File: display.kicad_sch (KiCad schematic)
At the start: 32 parts, among them Q1 AO3401A, Q2 BSS138

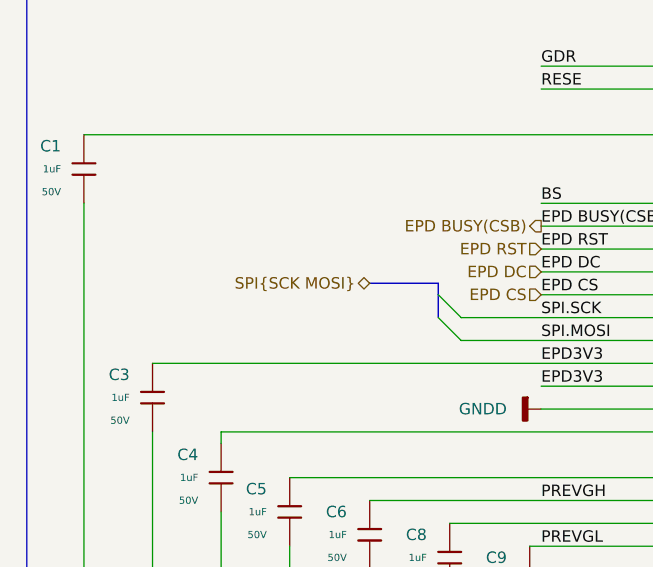
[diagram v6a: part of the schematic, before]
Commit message: Changed some parts for more common ones
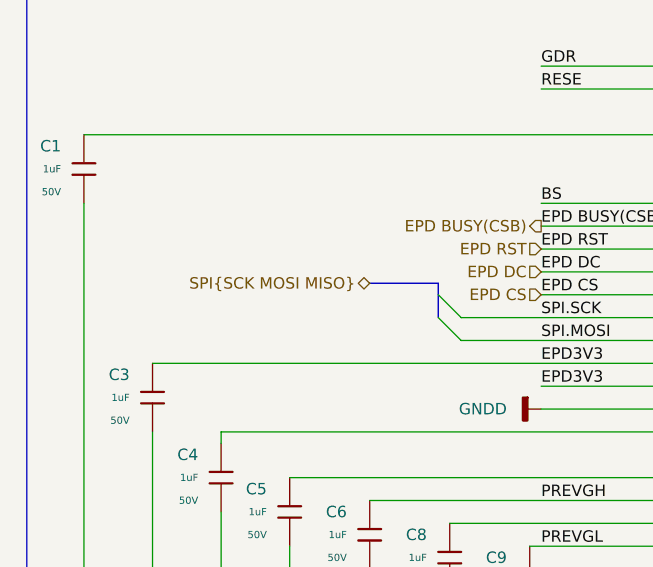
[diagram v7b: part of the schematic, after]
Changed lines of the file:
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@@
 		)
 	)
-	(hierarchical_label "SPI{SCK MOSI}"
+	(hierarchical_label "SPI{SCK MOSI MISO}"
 		(shape bidirectional)
 		(at 55.88 152.4 180)
@@
 		(dnp no)
 		(fields_autoplaced yes)
-		(property "Reference" "#PWR02"
+		(property "Reference" "#PWR03"
 			(at 49.53 118.11 0)
 			(effects
@@
 			(project "E-paper-picture-frame-HW"
 				(path "/84f37c25-92ec-4cd3-b0ad-d93e10e73cdb/9b514820-994d-4acc-ba3e-efc41ebe2f4e"
-					(reference "#PWR02")
+					(reference "#PWR03")
 					(unit 1)
 				)
@@
 		(dnp no)
 		(fields_autoplaced yes)
-		(property "Reference" "#PWR08"
+		(property "Reference" "#PWR09"
 			(at 95.25 33.02 0)
 			(effects
@@
 			(project ""
 				(path "/84f37c25-92ec-4cd3-b0ad-d93e10e73cdb/9b514820-994d-4acc-ba3e-efc41ebe2f4e"
-					(reference "#PWR08")
+					(reference "#PWR09")
 					(unit 1)
 				)
@@
 		(dnp no)
 		(fields_autoplaced yes)
-		(property "Reference" "#PWR06"
+		(property "Reference" "#PWR07"
 			(at 80.01 66.04 0)
 			(effects
@@
 			(project "E-paper-picture-frame-HW"
 				(path "/84f37c25-92ec-4cd3-b0ad-d93e10e73cdb/9b514820-994d-4acc-ba3e-efc41ebe2f4e"
-					(reference "#PWR06")
+					(reference "#PWR07")
 					(unit 1)
 				)
@@
 		(dnp no)
 		(fields_autoplaced yes)
-		(property "Reference" "#PWR011"
+		(property "Reference" "#PWR012"
 			(at 109.22 57.15 0)
 			(effects
@@
 			(project "E-paper-picture-frame-HW"
 				(path "/84f37c25-92ec-4cd3-b0ad-d93e10e73cdb/9b514820-994d-4acc-ba3e-efc41ebe2f4e"
-					(reference "#PWR011")
+					(reference "#PWR012")
 					(unit 1)
 				)
@@
 		(dnp no)
 		(fields_autoplaced yes)
-		(property "Reference" "#PWR04"
+		(property "Reference" "#PWR05"
 			(at 58.42 198.12 0)
 			(effects
@@
 			(project "E-paper-picture-frame-HW"
 				(path "/84f37c25-92ec-4cd3-b0ad-d93e10e73cdb/9b514820-994d-4acc-ba3e-efc41ebe2f4e"
-					(reference "#PWR04")
+					(reference "#PWR05")
 					(unit 1)
 				)
@@
 		(on_board yes)
 		(dnp no)
-		(property "Reference" "#PWR09"
+		(property "Reference" "#PWR010"
 			(at 105.41 114.3 0)
 			(effects
@@
 			(project "E-paper-picture-frame-HW"
 				(path "/84f37c25-92ec-4cd3-b0ad-d93e10e73cdb/9b514820-994d-4acc-ba3e-efc41ebe2f4e"
-					(reference "#PWR09")
+					(reference "#PWR010")
 					(unit 1)
 				)
@@
 		(dnp no)
 		(fields_autoplaced yes)
-		(property "Reference" "#PWR012"
+		(property "Reference" "#PWR013"
 			(at 143.51 46.99 0)
 			(effects
@@
 			(project "E-paper-picture-frame-HW"
 				(path "/84f37c25-92ec-4cd3-b0ad-d93e10e73cdb/9b514820-994d-4acc-ba3e-efc41ebe2f4e"
-					(reference "#PWR012")
+					(reference "#PWR013")
 					(unit 1)
 				)
@@
 		(dnp no)
 		(fields_autoplaced yes)
-		(property "Reference" "#PWR03"
+		(property "Reference" "#PWR04"
 			(at 53.34 26.67 0)
 			(effects
@@
 			(project ""
 				(path "/84f37c25-92ec-4cd3-b0ad-d93e10e73cdb/9b514820-994d-4acc-ba3e-efc41ebe2f4e"
-					(reference "#PWR03")
+					(reference "#PWR04")
 					(unit 1)
 				)
@@
 		(dnp no)
 		(fields_autoplaced yes)
-		(property "Reference" "#PWR01"
+		(property "Reference" "#PWR02"
 			(at 27.94 118.11 0)
 			(effects
@@
 			(project "E-paper-picture-frame-HW"
 				(path "/84f37c25-92ec-4cd3-b0ad-d93e10e73cdb/9b514820-994d-4acc-ba3e-efc41ebe2f4e"
-					(reference "#PWR01")
+					(reference "#PWR02")
 					(unit 1)
 				)
@@
 		(dnp no)
 		(fields_autoplaced yes)
-		(property "Reference" "#PWR07"
+		(property "Reference" "#PWR08"
 			(at 68.58 166.37 0)
 			(effects
@@
 			(project "E-paper-picture-frame-HW"
 				(path "/84f37c25-92ec-4cd3-b0ad-d93e10e73cdb/9b514820-994d-4acc-ba3e-efc41ebe2f4e"
-					(reference "#PWR07")
+					(reference "#PWR08")
 					(unit 1)
 				)
@@
 		(dnp no)
 		(fields_autoplaced yes)
-		(property "Reference" "#PWR010"
+		(property "Reference" "#PWR011"
 			(at 105.41 195.58 0)
 			(effects
@@
 			(project "E-paper-picture-frame-HW"
 				(path "/84f37c25-92ec-4cd3-b0ad-d93e10e73cdb/9b514820-994d-4acc-ba3e-efc41ebe2f4e"
-					(reference "#PWR010")
+					(reference "#PWR011")
 					(unit 1)
 				)
@@
 		(dnp no)
 		(fields_autoplaced yes)
-		(property "Reference" "#PWR05"
+		(property "Reference" "#PWR06"
 			(at 73.66 35.56 0)
 			(effects
@@
 			(project ""
 				(path "/84f37c25-92ec-4cd3-b0ad-d93e10e73cdb/9b514820-994d-4acc-ba3e-efc41ebe2f4e"
-					(reference "#PWR05")
+					(reference "#PWR06")
 					(unit 1)
 				)

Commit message: Finished USB, SD card and Power Mmt layout
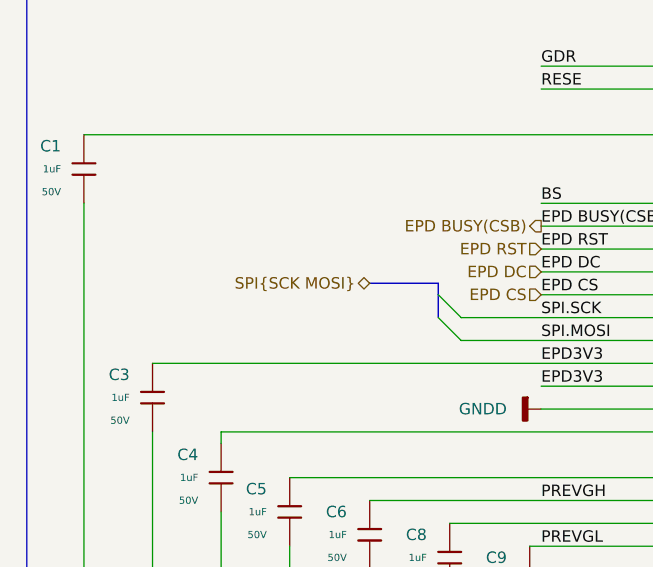
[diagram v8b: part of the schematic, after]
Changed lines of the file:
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@@
 		)
 	)
-	(hierarchical_label "SPI{SCK MOSI MISO}"
+	(hierarchical_label "SPI{SCK MOSI}"
 		(shape bidirectional)
 		(at 55.88 152.4 180)
